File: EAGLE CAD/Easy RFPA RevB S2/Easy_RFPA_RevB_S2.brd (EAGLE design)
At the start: 152.4 x 152.4 mm, 197 parts, among them IC301 74AHC1G14DBV, IC302 LM324D, J401 FUSE_2P, J402 KK_PCFAN, Q101 IRF520N, Q102 IRF630, Q201 IRF630, Q202 IRF630, Q301 BSS123, T101 HP4_TRAFO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

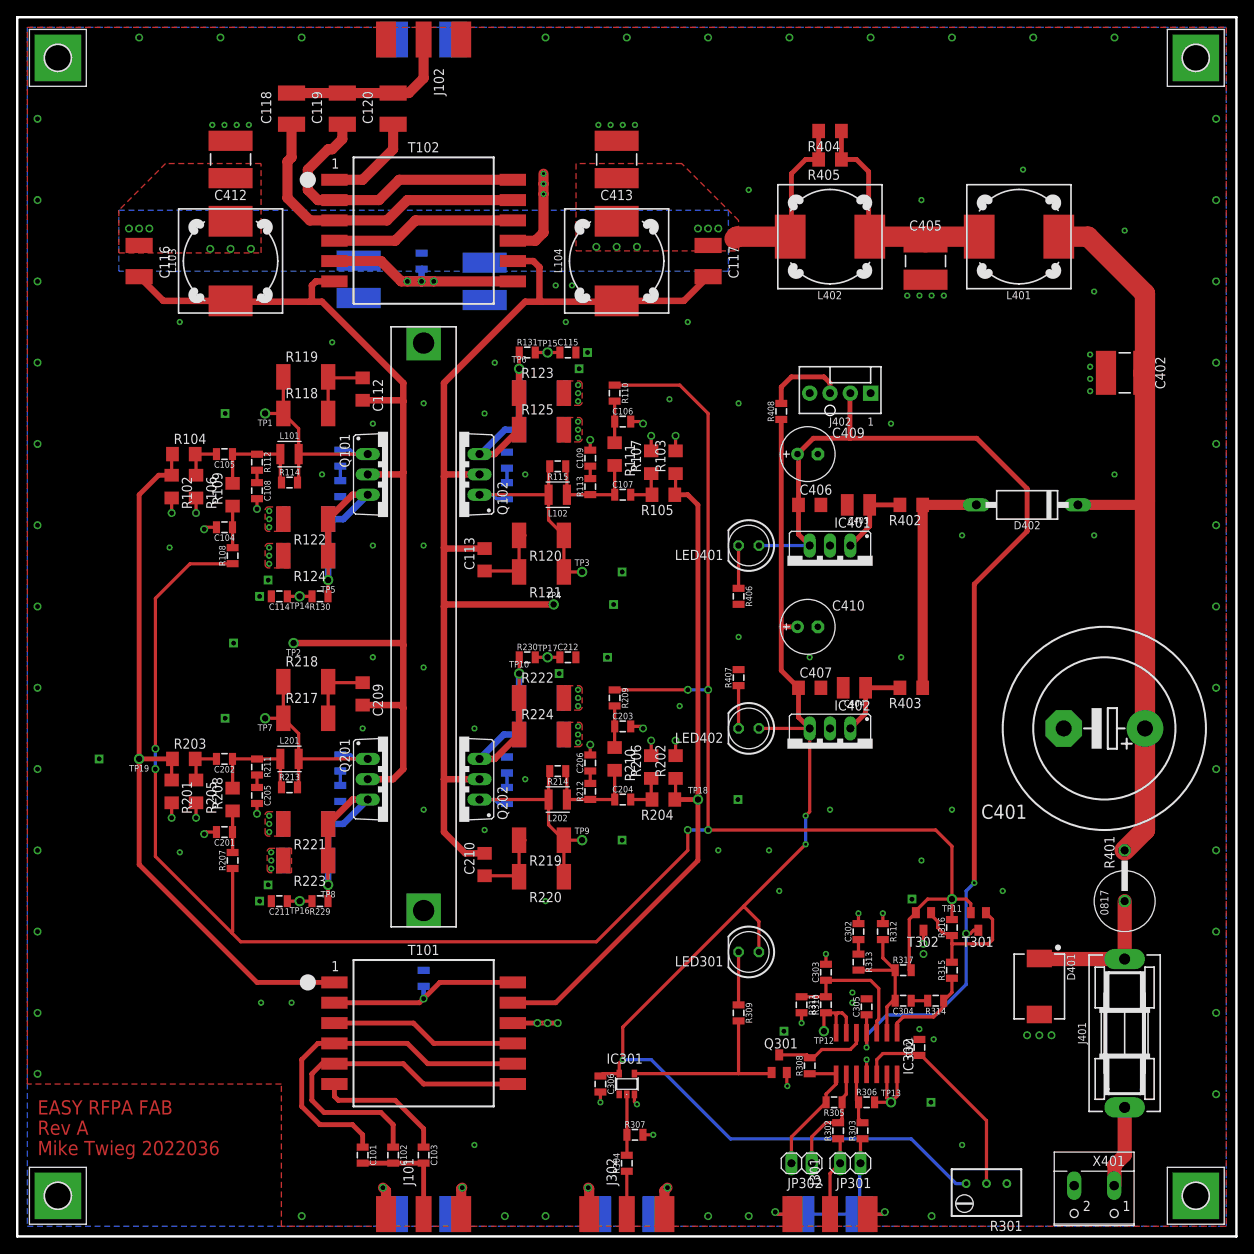
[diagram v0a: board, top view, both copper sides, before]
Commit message: Copy revA S2 to new revB S2
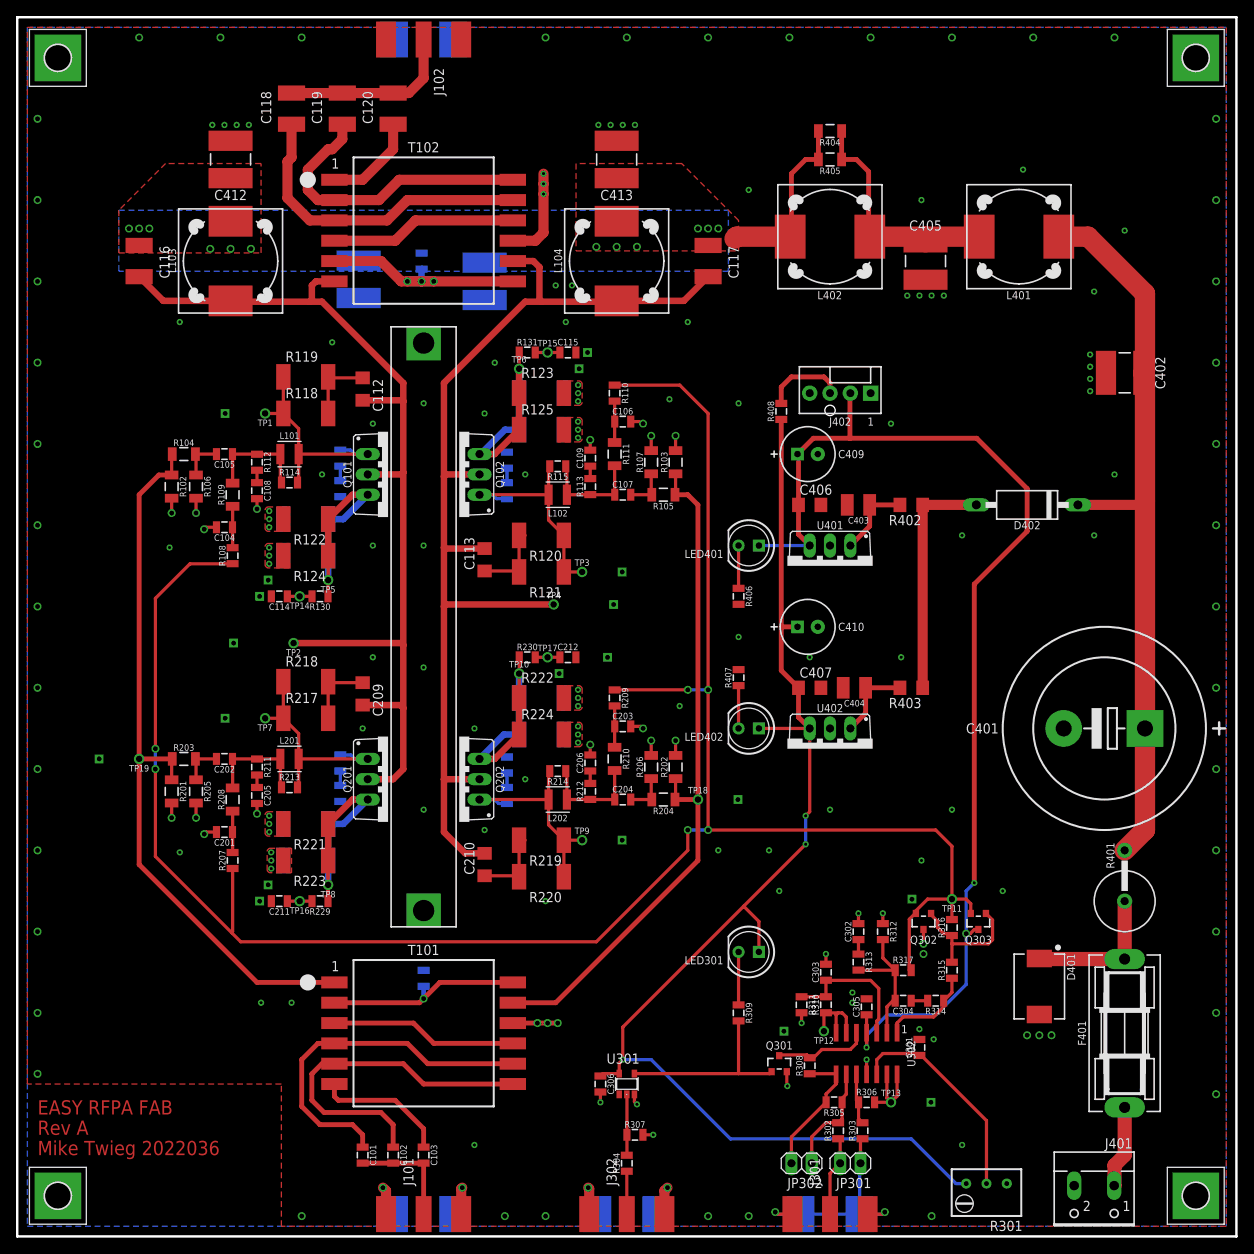
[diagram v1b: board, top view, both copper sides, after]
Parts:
- removed IC302: LM324D, linear:SO14
- removed IC401, IC402: (no value), v-reg:78XXS
- removed T301, T302: (no value), transistor:SOT23-BEC
- removed X401: (no value), con-wago-500:W237-102
- added F401: FUSE_2P, MDT_FUSE:02540121Z
- added Q302: PNPSOT23_BEC, MDT_TRANS:SOT23R_INFINEON
- added Q303: NPNMMBT3904SOT23_BEC, MDT_TRANS:SOT23R_INFINEON
- added U302: OPAMP_QUADTLV274IDSOIC14, MDT_IC:SO14
- added U401: LDO_3TERMMC78M12CTGTO220_VERT, MDT_IC:TO220BV
- added U402: LDO_3TERMMC78M05CTGTO220_VERT, MDT_IC:TO220BV
- C101, C102, C108, C109, C110, C111, C116, C117, C118, C119, C205, C206, C207, C208, C302, C303: value 0.1uF -> DNP
- C103, C120: value 0.1uF -> 3nF
- C104, C106, C201, C203: value 0.1uF -> 22nF
- C105, C107, C202, C204: value 0.1uF -> 27nF
- C112, C113, C209, C210: value 22nF -> 2.2nF
- C114, C115, C211, C212: value 0.1uF -> 10nF
- C304: value 0.1uF -> 33pF
- C401: device rcl:EB25D -> MDT_C:EB25D
- C406, C407: value 47nF -> 4.7uF
- C409, C410: device rcl:E2,5-7 -> MDT_C:E2,5-7
- J101, J102, J301, J302: value (none) -> COAX112640BNC_EDGE
- J401: value FUSE_2P -> HDR_2X1282836-1282836-1; device MDT_FUSE:02540121Z -> MDT_CON:W237-02
- L101, L102, L201, L202: value 1uH -> 47nH
- L103, L104: value (none) -> 3.3uH
- LED301: value (none) -> LEDHLMP-3401-E0002T1_3/4; device led:LED5MM -> MDT_Diode:LED5MM
- LED401, LED402: value (none) -> LEDHLMP-3962-F0002T1_3/4; device led:LED5MM -> MDT_Diode:LED5MM
- Q101, Q102, Q201, Q202: device transistor-power:TO220BV -> MDT_TRANS:TO220BV
- Q301: value BSS123 -> MOSFET_NBSS123SOT23; device transistor-small-signal:SOT23 -> MDT_TRANS:SOT23R_INFINEON
- R101, R132, R314: value 1.0K -> 0
- R102, R103, R106, R107, R201, R202, R205, R206: value 1K -> 75; device MDT_R:R1206 -> MDT_R:1206_IPC-7351B
- R104, R105, R203, R204: value 1K -> 4.99; device MDT_R:R1206 -> MDT_R:1206_IPC-7351B
- R108, R110, R207, R209, R316: value 1.0K -> 100
- R109, R111, R208, R210: value 1K -> 100; device MDT_R:R1206 -> MDT_R:1206_IPC-7351B
- R112, R113, R116, R117, R211, R212, R215, R216, R311, R313: value 1.0K -> DNP
- R114, R115, R213, R214: value 1.0K -> 15
- R118, R120, R217, R219: value 1K -> 330
- R119, R121, R218, R220: value 1K -> 270
- R122, R123, R124, R125, R126, R127, R221, R222, R223, R224, R225, R226: value 1K -> 2.7
- R128, R129, R227, R228: value 1K -> 3.3
- R130, R131, R229, R230, R304, R308, R310: value 1.0K -> 1K
- R301: device rcl:RTRIM3299W -> MDT_R:RTRIM3299W
- R302, R303, R305, R306, R312, R317: value 1.0K -> 10K
- R307: value 1.0K -> 100K
- R309: value 1.0K -> 150
- R315: value 1.0K -> 10
- R401: device resistor:P0817V -> MDT_R:P0817V
- R404, R405: device MDT_R:R1206 -> MDT_R:1206_IPC-7351B
- X402: value HEATSINK_OMNI_DUAL30-75-D -> HEATSINK_OMNI_DUALOMNI-UNI-30-75-D30-75-D
- moved J401 20.7 mm to (134.6, 5.08), turned to 180 degrees
- renumbered IC301 to U301
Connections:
- net +12V: now also Q303.3, U302.4, U401.3; no longer IC302.4, IC401.OUT, T301.C
- net +5V: now also U402.3; no longer IC402.OUT
- net GBIAS: now also Q302.2, Q303.2; no longer T301.E, T302.E
- net GND: now also J401.2, Q302.3, U302.11, U401.2, U402.2; no longer IC302.11, IC401.GND, IC402.GND, T302.C, X401.2
- net N$1: now also U302.1; no longer IC302.1
- net N$14: now also U302.2; no longer IC302.2
- net N$15: now also U302.3; no longer IC302.3
- net N$16: now also U302.10; no longer IC302.10
- net N$18: now also U302.8; no longer IC302.8
- net N$19: now also U302.9; no longer IC302.9
- net N$2: now also Q302.1, Q303.1; no longer T301.B, T302.B
- net N$23: now also U302.5; no longer IC302.5
- net N$25: now also U302.12; no longer IC302.12
- net N$26: now also U302.13, U302.14; no longer IC302.13, IC302.14
- net N$43: now also U401.1; no longer IC401.IN
- net N$44: now also F401.2; no longer J401.2
- net N$45: now also F401.1; no longer X401.1
- net N$49: now also U402.1; no longer IC402.IN
- net N$6: now also U302.6, U302.7; no longer IC302.6, IC302.7

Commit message: Work on revB
revB is basically the same as revA, except will have soldermask and silkscreen. Some components are moved around to make room for labels. Name labels updated in libraries.
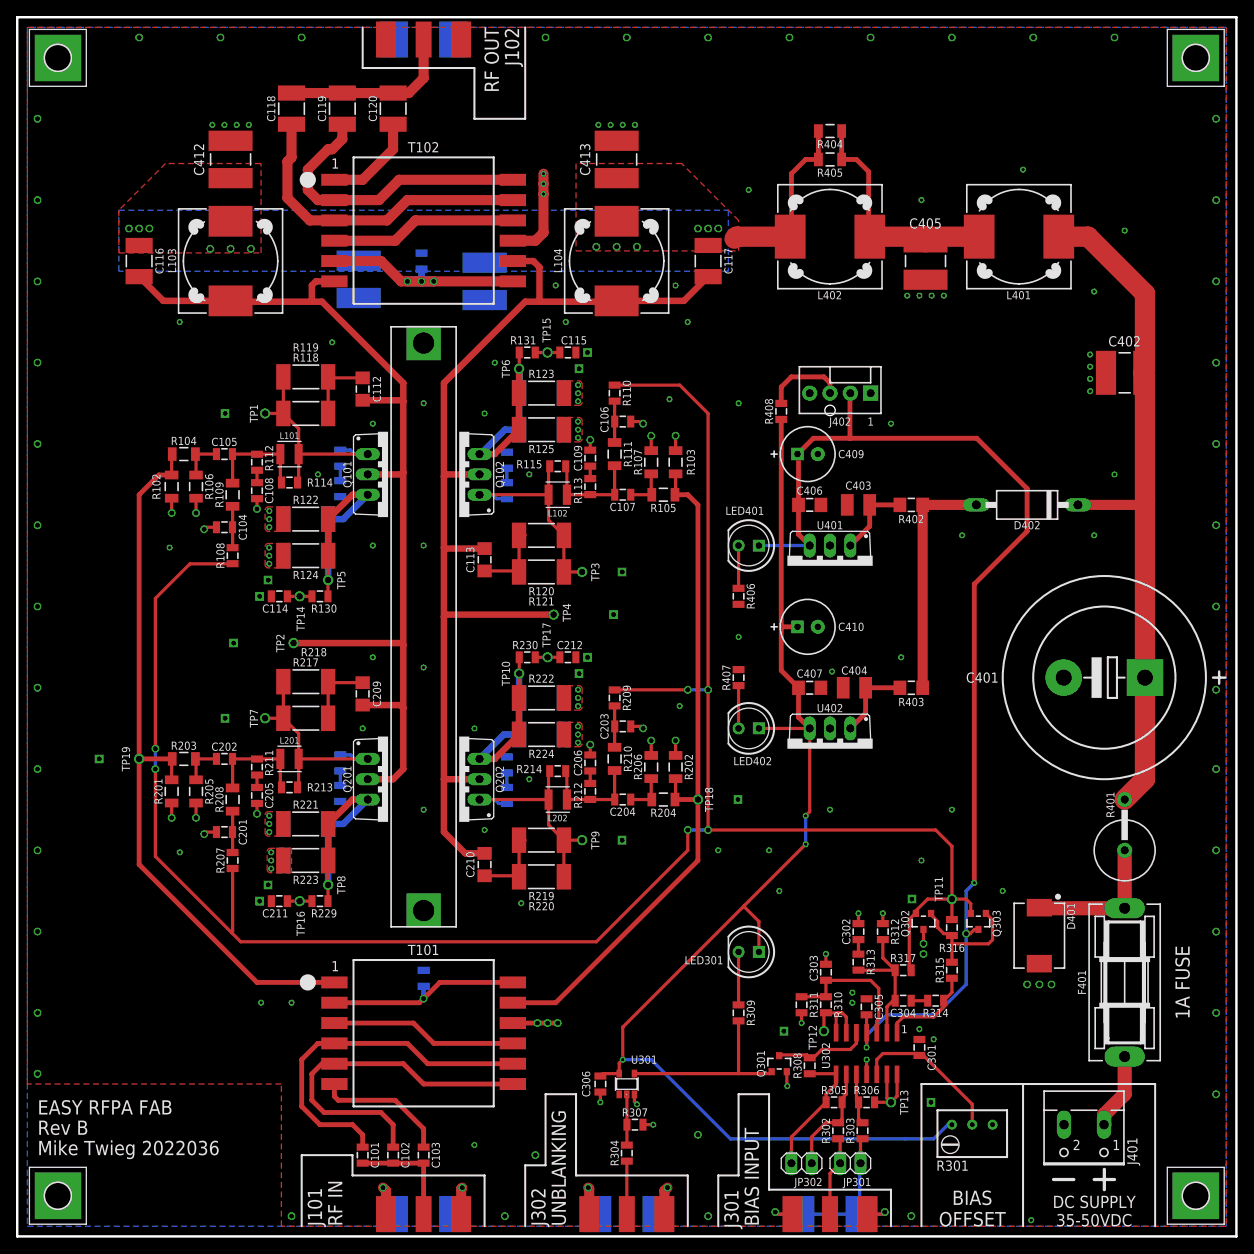
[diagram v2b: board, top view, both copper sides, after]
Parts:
- TP10: value PROBE_TPTP_5MM -> PROBE_TPTP_7P5MM; device MDT_CON:PROBE_TP_5MM -> MDT_CON:PROBE_TP_7P5MM
- TP17: value PROBE_TPTP_7P5MM -> PROBE_TPTP_5MM; device MDT_CON:PROBE_TP_7P5MM -> MDT_CON:PROBE_TP_5MM
- moved J401 7.73 mm to (133.3, 12.7)
- moved R301 7.58 mm to (119.4, 12.7)
- moved F401 6.35 mm to (138.4, 31.8)
- moved R401 6.35 mm to (138.4, 53.3)
- moved D401 6.35 mm to (127.8, 37.6)
- moved C401 6.35 mm to (135.9, 69.8)
- moved R307 1.27 mm to (77.2, 14.0)
- moved R304 1.27 mm to (76.2, 10.4)
- moved TP4 1.27 mm to (67.1, 77.7)
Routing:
- net N$25: track 27.2 -> 19.3 mm
- net N$46: track 93.1 -> 86.8 mm
- net +5V: track 159.8 -> 156.5 mm
- net BP5: track 31.7 -> 29.7 mm
- net N$53: track 5.35 -> 6.62 mm
- net N$3: track 7.63 -> 6.36 mm
- net N$45: track 10.3 -> 9.60 mm
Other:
- board text added: "1A FUSE"
- board text added: "BIAS INPUT"
- board text added: "BIAS OFFSET"
- board text added: "DC SUPPLY 35-50VDC"
- board text added: "RF IN"
- board text added: "RF OUT"
- board text added: "Rev B"
- board text added: "UNBLANKING"
- board text removed: "Rev A"
